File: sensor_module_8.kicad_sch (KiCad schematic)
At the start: 26 parts, among them J1 Conn_Coaxial, J3 Conn_Coaxial, J4 Conn_Coaxial, J5 Conn_Coaxial, U12 REF3025, U13 MCP3204, U16 INA333xxDGK, U17 INA333xxDGK, U18 INA333xxDGK, U19 INA333xxDGK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

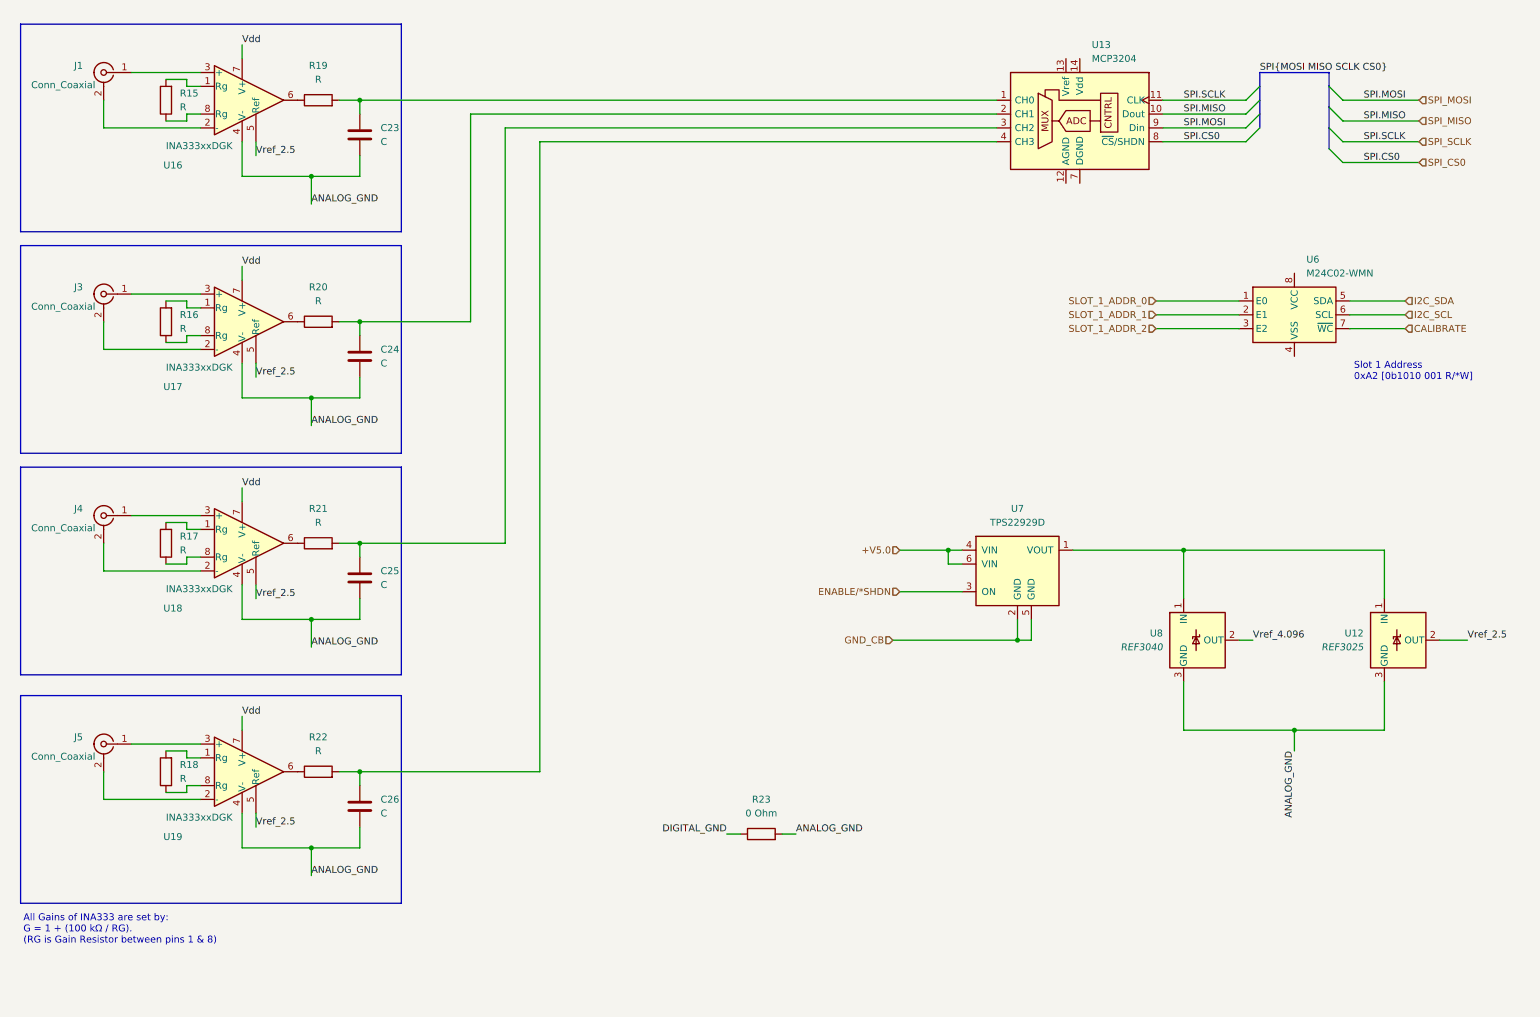
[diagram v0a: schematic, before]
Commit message: Split the sensor modules into a 4 and 8 port version. Fleshed out the power module a bit more. Started adding sensor board connectors to the root schematic and started pulling out sensor boards to their own, separate module. Began wiring up the root schematic to get my bearings a bit.
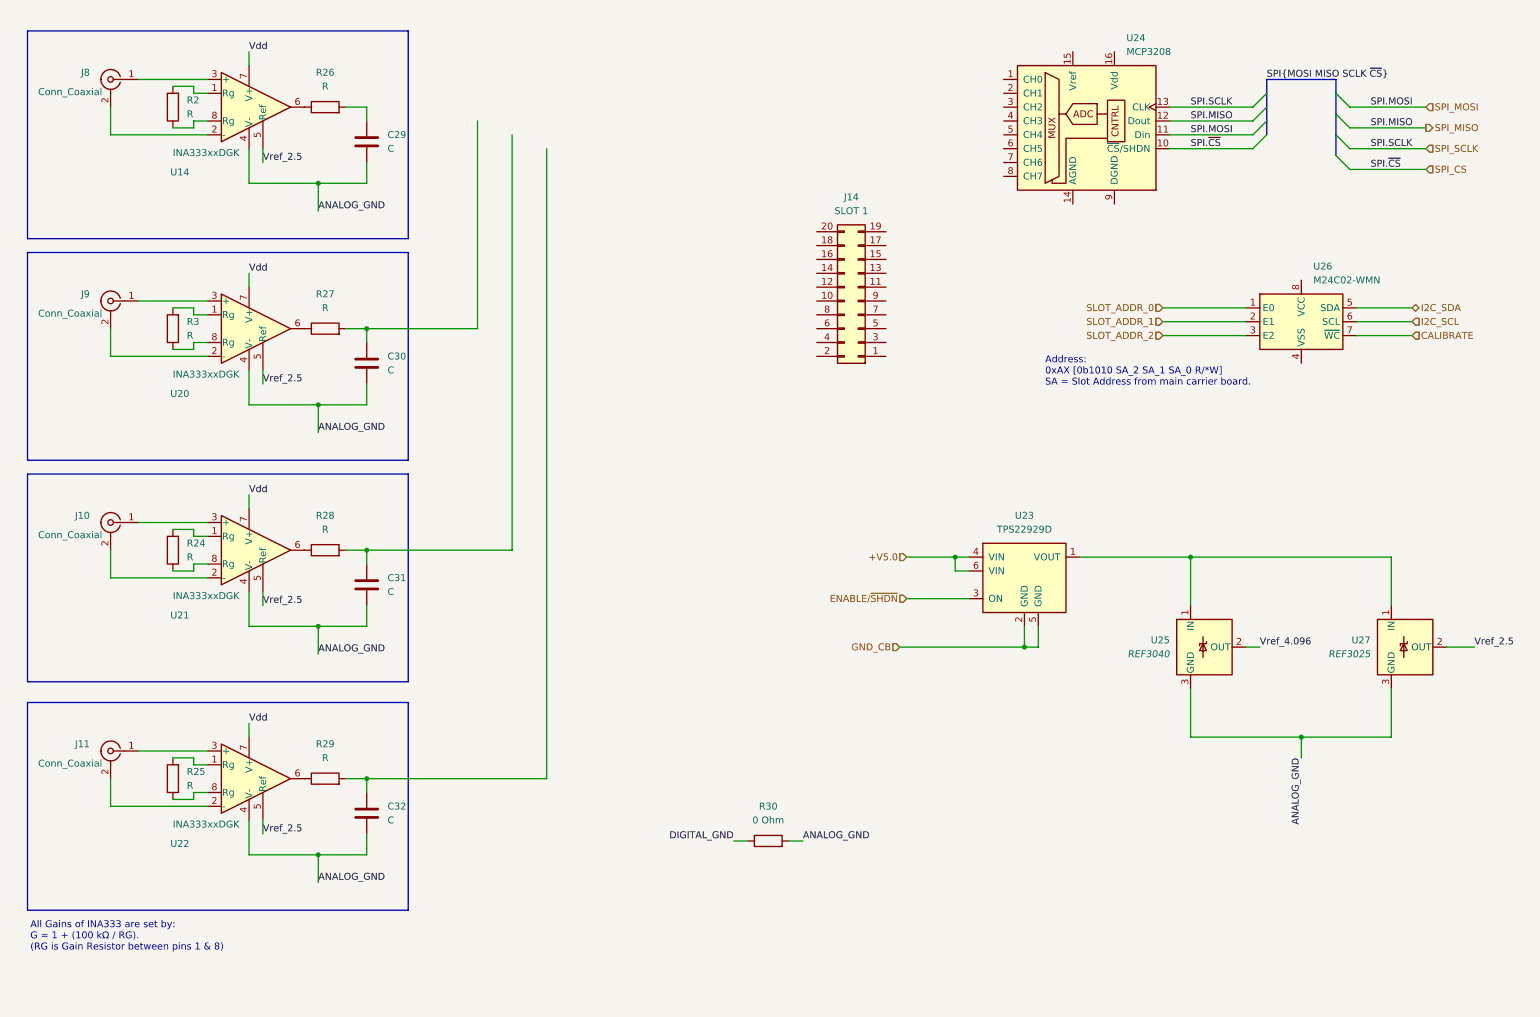
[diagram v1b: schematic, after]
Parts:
- removed C23, C24, C25, C26: C, symbol Device:C
- removed J1, J3, J4, J5: Conn_Coaxial, symbol Connector:Conn_Coaxial
- removed R15, R16, R17, R18, R19, R20, R21, R22: R, symbol Device:R
- removed R23: 0 Ohm, symbol Device:R
- removed U12: REF3025, Package_TO_SOT_SMD:SOT-23, symbol Reference_Voltage:REF3025
- removed U13: MCP3204, symbol Analog_ADC:MCP3204
- removed U16, U17, U18, U19: INA333xxDGK, Package_SO:VSSOP-8_3x3mm_P0.65mm, symbol Amplifier_Instrumentation:INA333xxDGK
- removed U6: M24C02-WMN, Package_SO:SOIC-8_3.9x4.9mm_P1.27mm, symbol Memory_EEPROM:M24C02-WMN
- removed U7: TPS22929D, Package_TO_SOT_SMD:SOT-23-6, symbol Power_Management:TPS22929D
- removed U8: REF3040, Package_TO_SOT_SMD:SOT-23, symbol Reference_Voltage:REF3040
- added C29, C30, C31, C32: C, symbol Device:C
- added J10, J11, J8, J9: Conn_Coaxial, symbol Connector:Conn_Coaxial
- added J14: SLOT 1, symbol Connector_Generic:Conn_02x10_Odd_Even
- added R2, R24, R25, R26, R27, R28, R29, R3: R, symbol Device:R
- added R30: 0 Ohm, symbol Device:R
- added U14, U20, U21, U22: INA333xxDGK, Package_SO:VSSOP-8_3x3mm_P0.65mm, symbol Amplifier_Instrumentation:INA333xxDGK
- added U23: TPS22929D, Package_TO_SOT_SMD:SOT-23-6, symbol Power_Management:TPS22929D
- added U24: MCP3208, symbol Analog_ADC:MCP3208
- added U25: REF3040, Package_TO_SOT_SMD:SOT-23, symbol Reference_Voltage:REF3040
- added U26: M24C02-WMN, Package_SO:SOIC-8_3.9x4.9mm_P1.27mm, symbol Memory_EEPROM:M24C02-WMN
- added U27: REF3025, Package_TO_SOT_SMD:SOT-23, symbol Reference_Voltage:REF3025
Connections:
- net +V5.0: now also U23.4 (VIN), U23.6 (VIN)
- net ANALOG_GND: now also C29.2, C30.2, C31.2, C32.2, R30.2, U14.4 (V-), U20.4 (V-), U21.4 (V-), U22.4 (V-), U25.3 (GND), U27.3 (GND)
- net CALIBRATE: now also U26.7 (~{WC})
- net DIGITAL_GND: now also R30.1
- net GND_CB: now also U23.2 (GND), U23.5 (GND)
- net I2C_SCL: now also U26.6 (SCL)
- net I2C_SDA: now also U26.5 (SDA)
- net SPI_MISO: now also U24.12 (Dout)
- net SPI_MOSI: now also U24.11 (Din)
- net SPI_SCLK: now also U24.13 (CLK)
- net Vdd: now also U14.7 (V+), U20.7 (V+), U21.7 (V+), U22.7 (V+)
- net Vref_2.5: now also U14.5 (Ref), U20.5 (Ref), U21.5 (Ref), U22.5 (Ref), U27.2 (OUT)
- net Vref_4.096: now also U25.2 (OUT)
- new net: R2.2, U14.1 (Rg)
- new net: J8.2 (Ext), U14.2 (-)
- new net: J8.1 (In), U14.3 (+)
- new net: R26.1, U14.6
- new net: R2.1, U14.8 (Rg)
- new net: R25.1, U22.8 (Rg)
- new net: R25.2, U22.1 (Rg)
- new net: U23.1 (VOUT), U25.1 (IN), U27.1 (IN)
- new net: C31.1, R28.2
- new net: C29.1, R26.2
- new net: R28.1, U21.6
- new net: R3.1, U20.8 (Rg)
- new net: R3.2, U20.1 (Rg)
- new net: J11.1 (In), U22.3 (+)
- new net: J11.2 (Ext), U22.2 (-)
- new net: R27.1, U20.6
- new net: C30.1, R27.2
- new net: J9.2 (Ext), U20.2 (-)
- new net: J9.1 (In), U20.3 (+)
- new net: R24.2, U21.1 (Rg)
- new net: J10.2 (Ext), U21.2 (-)
- new net: J10.1 (In), U21.3 (+)
- new net: R24.1, U21.8 (Rg)
- new net: R29.1, U22.6
- new net: C32.1, R29.2
- new net ENABLE/~{SHDN}: U23.3 (ON)
- new net SLOT_ADDR_0: U26.1 (E0)
- new net SLOT_ADDR_1: U26.2 (E1)
- new net SLOT_ADDR_2: U26.3 (E2)
- new net SPI_CS: U24.10 (~{CS}/SHDN)
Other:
- note added: "Address: 0xAX [0b1010 SA_2 SA_1 SA_0 R/*W] SA = Slot Address from main carrier board."
- note removed: "Slot 1 Address 0xA2 [0b1010 001 R/*W]"

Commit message: Removed hierarchical labels on the sensor board (4 slot) in favour of local labels and connectors. The idea was that the sensor boards are plug-ins so having them defined as separate boards makes more sense. Eventually I think we'll pull them out of the main schematic and design each one separately with the common connector pinout.
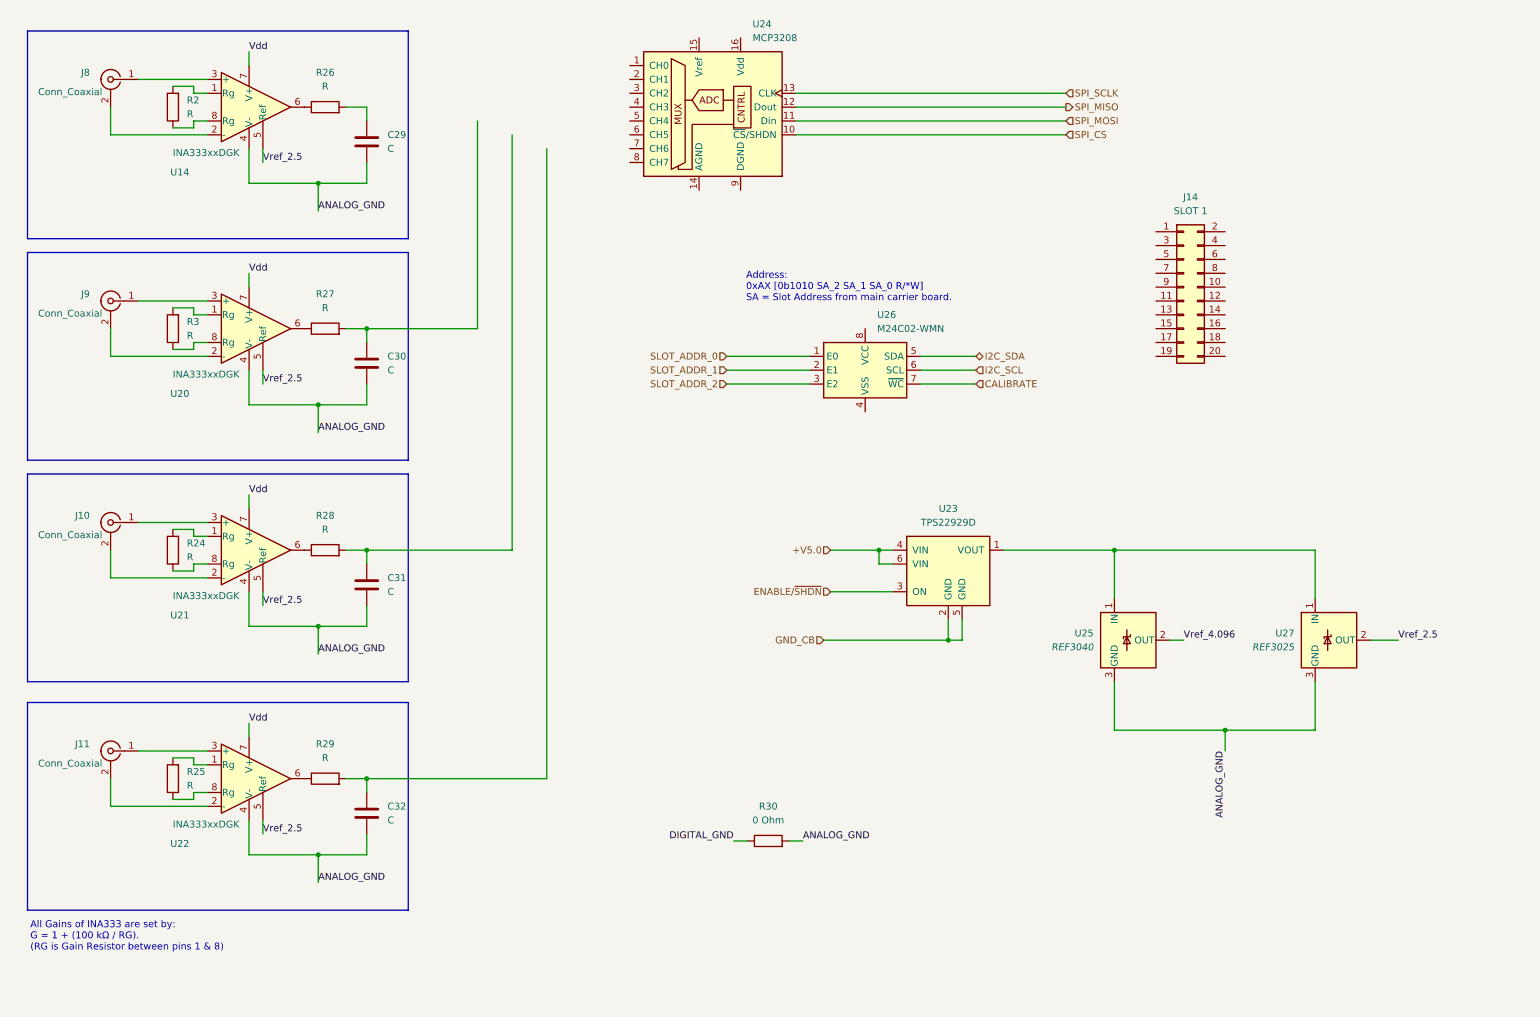
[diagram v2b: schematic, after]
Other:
- moved on the sheet: J14, U23, U24, U25, U26, U27

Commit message: Cleaned up some signal lines in the sensor board. Shuffled the decoupling caps around a bit as well as rearranged the EEPROM and power supply for clarity. Added buffered 2.5V offset to the pH and ORP circuits. Swapped one TBD input on the base sensor and sensor_4 boards for an ADC calibration input.
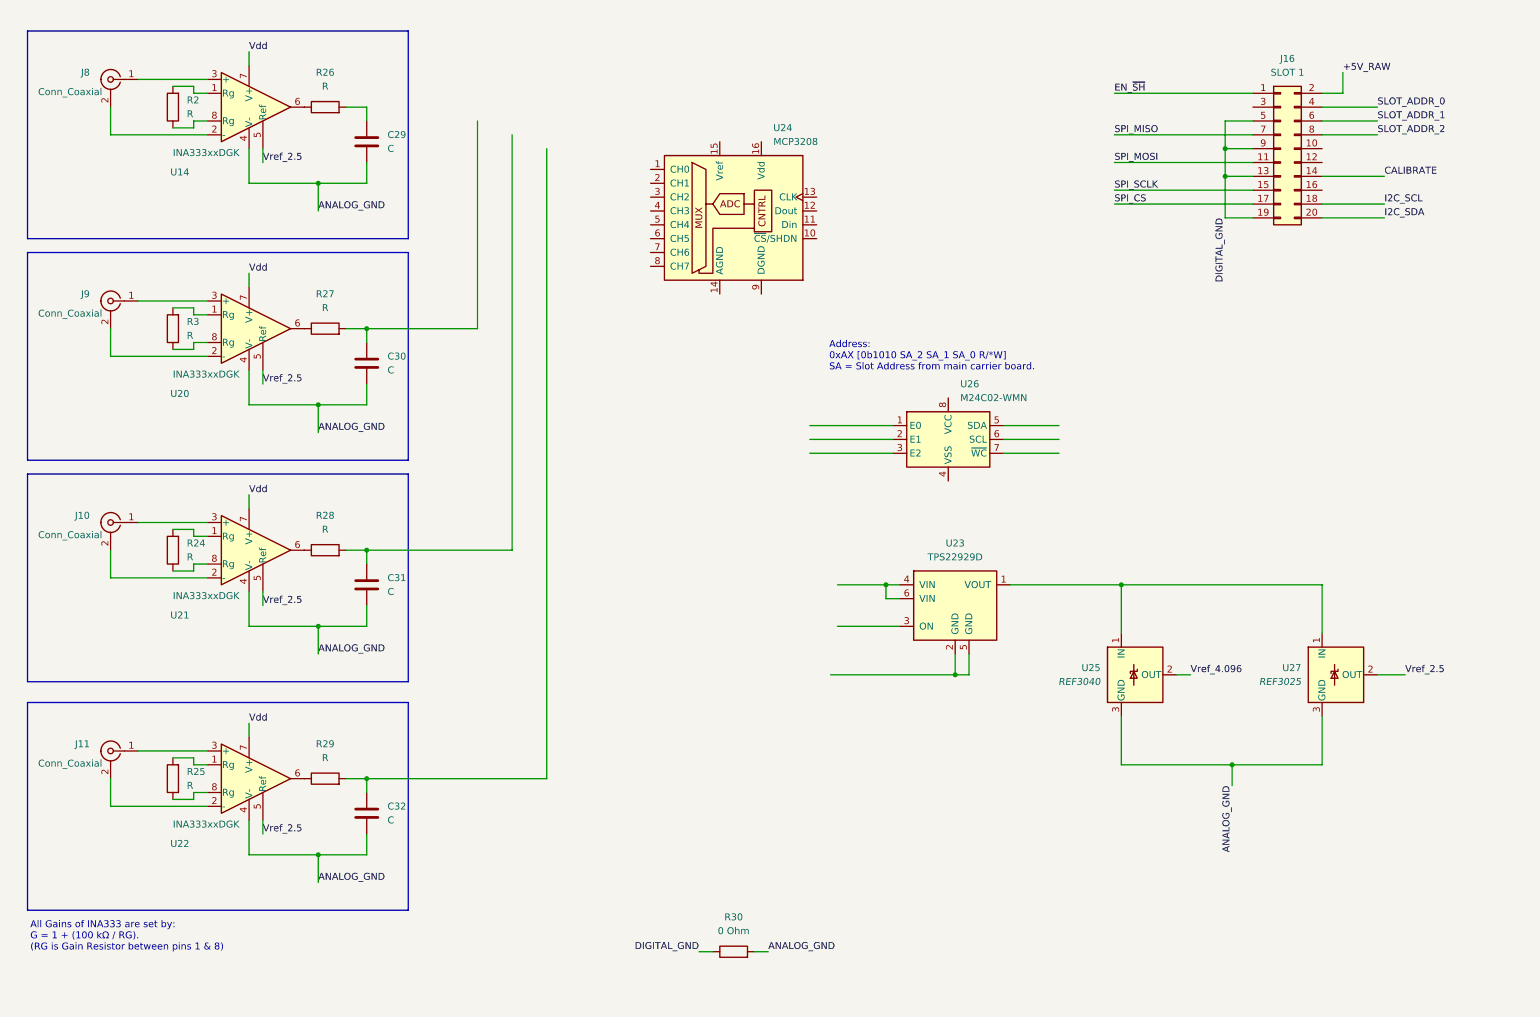
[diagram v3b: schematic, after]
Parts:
- removed J14: SLOT 1, symbol Connector_Generic:Conn_02x10_Odd_Even
- added J16: SLOT 1, symbol Connector_Generic:Conn_02x10_Odd_Even
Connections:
- net CALIBRATE: now also J16.14 (Pin_14); no longer U26.7 (~{WC})
- net DIGITAL_GND: now also J16.13 (Pin_13), J16.19 (Pin_19), J16.5 (Pin_5), J16.9 (Pin_9)
- net I2C_SCL: now also J16.18 (Pin_18); no longer U26.6 (SCL)
- net I2C_SDA: now also J16.20 (Pin_20); no longer U26.5 (SDA)
- net SLOT_ADDR_0: now also J16.4 (Pin_4); no longer U26.1 (E0)
- net SLOT_ADDR_1: now also J16.6 (Pin_6); no longer U26.2 (E1)
- net SLOT_ADDR_2: now also J16.8 (Pin_8); no longer U26.3 (E2)
- net SPI_CS: now also J16.17 (Pin_17); no longer U24.10 (~{CS}/SHDN)
- net SPI_MISO: now also J16.7 (Pin_7); no longer U24.12 (Dout)
- net SPI_MOSI: now also J16.11 (Pin_11); no longer U24.11 (Din)
- net SPI_SCLK: now also J16.15 (Pin_15); no longer U24.13 (CLK)
- net +V5.0: no longer names the net of U23.4 (VIN), U23.6 (VIN)
- net ENABLE/~{SHDN}: no longer names the net of U23.3 (ON)
- net GND_CB: no longer names the net of U23.2 (GND), U23.5 (GND)
- new net +5V_RAW: J16.2 (Pin_2)
- new net EN_~{SH}: J16.1 (Pin_1)
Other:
- moved on the sheet: R30, U23, U24, U25, U26, U27

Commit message: Added some notes to otherwise blank pages. Added the full 8 sensor buffers to the 8 sensor analog board. Added a decoupling sub page to same. Changed a couple of sensor labels on base and 4 board just as placeholders
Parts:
- added C58, C59, C60, C61: C, symbol Device:C
- added J17, J18, J19, J20: Conn_Coaxial, symbol Connector:Conn_Coaxial
- added R11, R18, R40, R41, R42, R43, R44, R45: R, symbol Device:R
- added U19, U28: OPA1678, symbol Amplifier_Operational:OPA1678
- added U30, U31, U32, U33: INA333xxDGK, Package_SO:VSSOP-8_3x3mm_P0.65mm, symbol Amplifier_Instrumentation:INA333xxDGK
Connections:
- net +5V_RAW is gone; now on net +5V: J16.2 (Pin_2)
- net ANALOG_GND: now also U24.14 (AGND), U24.9 (DGND), C58.2, C59.2, C60.2, C61.2, U28.4 (V-), U30.4 (V-), U31.4 (V-), U32.4 (V-), U33.4 (V-)
- net CALIBRATE: now also U26.7 (~{WC})
- net DIGITAL_GND: now also U23.2 (GND), U23.5 (GND), U26.4 (VSS)
- net EN_~{SH}: now also U23.3 (ON)
- net I2C_SCL: now also U26.6 (SCL)
- net I2C_SDA: now also U26.5 (SDA)
- net SLOT_ADDR_0: now also U26.1 (E0)
- net SLOT_ADDR_1: now also U26.2 (E1)
- net SLOT_ADDR_2: now also U26.3 (E2)
- net SPI_CS: now also U24.10 (~{CS}/SHDN)
- net SPI_MISO: now also U24.12 (Dout)
- net SPI_MOSI: now also U24.11 (Din)
- net SPI_SCLK: now also U24.13 (CLK)
- net Vdd: now also U23.1 (VOUT), U25.1 (IN), U26.8 (VCC), U27.1 (IN), U28.8 (V+), U30.7 (V+), U31.7 (V+), U32.7 (V+), U33.7 (V+)
- net Vref_2.5: now also U28.5 (+), U30.5 (Ref), U31.5 (Ref), U32.5 (Ref), U33.5 (Ref)
- net Vref_4.096: now also U24.16 (Vdd)
- net CH0: now reaches U24.1 (CH0)
- net CH0: now also C29.1, R26.2
- net Vref_2.5V: now reaches U24.15 (Vref)
- net CH1: now reaches U24.2 (CH1)
- net CH1: now also C30.1, R27.2
- net CH2: now reaches U24.3 (CH2)
- net CH2: now also C31.1, R28.2
- net CH3: now reaches U24.4 (CH3)
- net CH3: now also C32.1, R29.2
- net CH4: now reaches U24.5 (CH4)
- net CH4: now also C61.1, R45.2
- net CH5: now reaches U24.6 (CH5)
- net CH5: now also C60.1, R44.2
- net CH6: now reaches U24.7 (CH6)
- net CH6: now also C59.1, R43.2
- net CH7: now reaches U24.8 (CH7)
- net CH7: now also C58.1, R42.2
- net Vref_2.5_BUF: now reaches J8.2 (Ext), U14.2 (-)
- net Vref_2.5_BUF: now also J10.2 (Ext), J11.2 (Ext), J9.2 (Ext), U20.2 (-), U21.2 (-), U22.2 (-), U28.6 (-), U28.7
- net +5V: now reaches U23.4 (VIN), U23.6 (VIN)
- new net: R43.1, U31.6
- new net: R44.1, U32.6
- new net: R18.2, U31.1 (Rg)
- new net: J18.2 (Ext), U31.2 (-)
- new net: J18.1 (In), U31.3 (+)
- new net: R18.1, U31.8 (Rg)
- new net: R11.1, U30.8 (Rg)
- new net: R11.2, U30.1 (Rg)
- new net: R40.2, U32.1 (Rg)
- new net: J19.2 (Ext), U32.2 (-)
- new net: J19.1 (In), U32.3 (+)
- new net: R40.1, U32.8 (Rg)
- new net: R45.1, U33.6
- new net: J20.1 (In), U33.3 (+)
- new net: J20.2 (Ext), U33.2 (-)
- new net: J17.2 (Ext), U30.2 (-)
- new net: J17.1 (In), U30.3 (+)
- new net: R42.1, U30.6
- new net: R41.2, U33.1 (Rg)
- new net: R41.1, U33.8 (Rg)
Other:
- added sheet Sensor 8 decoupling (sensor_8_decoupling.kicad_sch)
- note added: "Spare"
- moved on the sheet: C29, C30, C31, C32, J10, J11, J16, J8, J9, R2, R24, R25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

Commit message: Oopsie. - Changed Channel 7 on the analog 8 board to a calibration input. - Added a TODO to the root page
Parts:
- removed C58: C, symbol Device:C
- removed R42: R, symbol Device:R
- removed U30: INA333xxDGK, Package_SO:VSSOP-8_3x3mm_P0.65mm, symbol Amplifier_Instrumentation:INA333xxDGK
- added C86: C, symbol Device:C
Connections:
- net ANALOG_GND: now also J17.2 (Ext), C86.2
- net CH7: now also R11.2, C86.1
- net at R11.1: now also J17.1 (In)
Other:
- note added: "Calibration Input"
